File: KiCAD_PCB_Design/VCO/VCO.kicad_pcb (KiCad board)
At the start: 2 copper layers, 40 x 33 mm, 6 parts, among them P1 SMA, P2 CONN_01X02, P3 SMA, U1 HMC38X

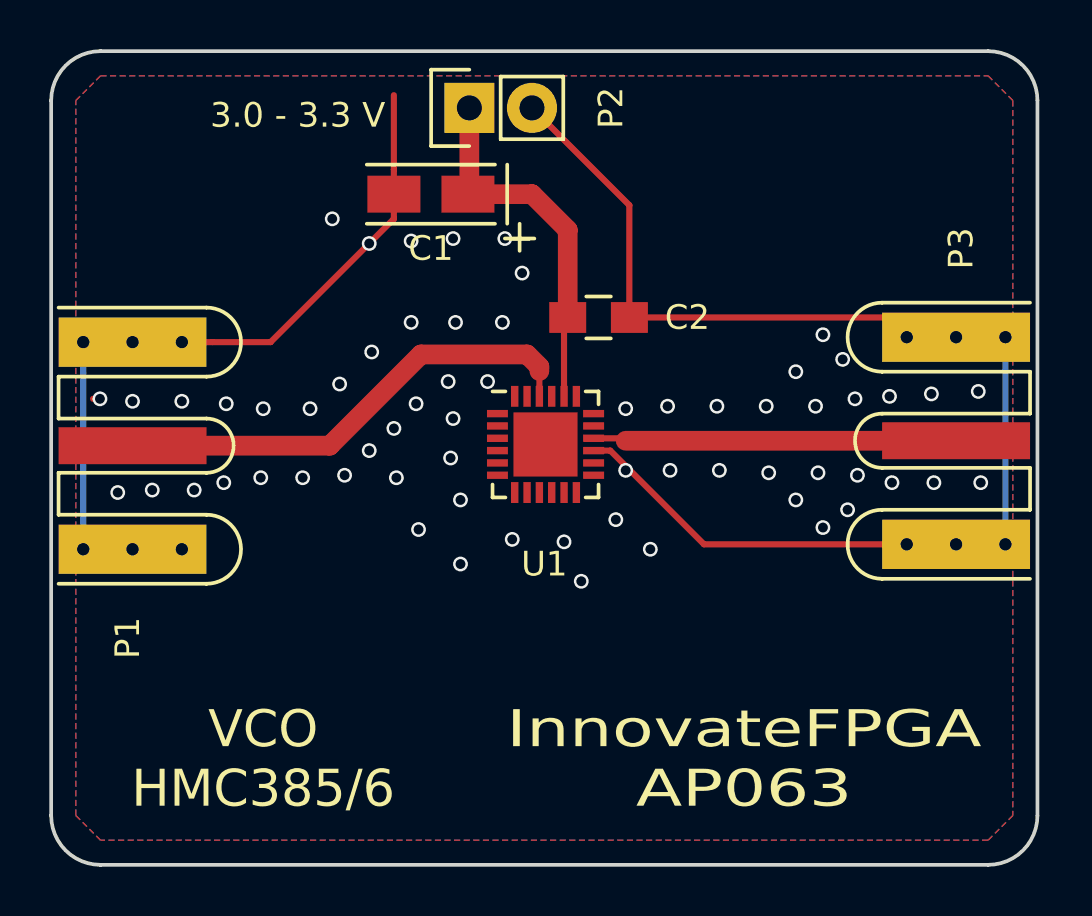
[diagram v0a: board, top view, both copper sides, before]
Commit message: All components made except antenna, Now verifying ..
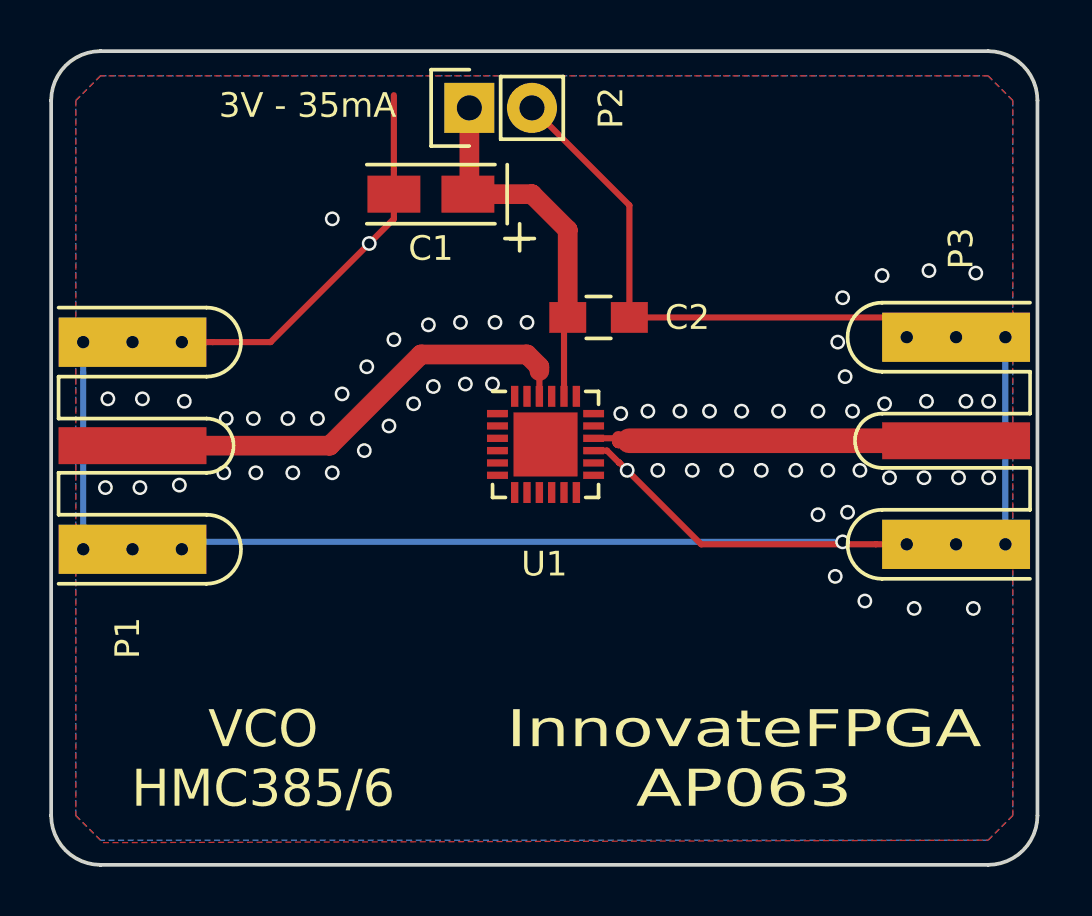
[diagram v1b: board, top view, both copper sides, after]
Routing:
- net GND: track 85.4 -> 112.2 mm, vias 2 -> 3
- net (no net): track 0.66 -> 1.30 mm, vias 62 -> 63
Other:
- board text added: "3V - 35mA"
- board text added: "FYP-2 MNNIT Allahabad Team 40 Batch 2k18"
- board text removed: "3.0 - 3.3 V"
- board text removed: "FYP-2 MNNIT Allahabad Team 40 2017-18"
